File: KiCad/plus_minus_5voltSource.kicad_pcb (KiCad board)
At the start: 2 copper layers, 31.1 x 16.2 mm, 9 parts, among them P1 CONN_01X03, U1 7660

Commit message: Removed old PCB layout from the pcb file.
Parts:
- removed C1, C2: CP, Capacitors_ThroughHole:C_Radial_D5_L6_P2.5
- removed D1, D2: LED, LEDs:LED_0805
- removed G***: LOGO, PCB:AVO Logo
- removed P1: CONN_01X03, Pin_Headers:Pin_Header_Angled_1x03
- removed R1, R2: 1k, Resistors_SMD:R_0805_HandSoldering
- removed U1: 7660, Housings_DIP:DIP-8_W7.62mm
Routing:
- net GND: track 41.4 -> 0.00 mm
- net V-: track 31.6 -> 0.00 mm
- net Net-(D2-Pad2): track 20.2 -> 0.00 mm
- net VCC: track 15.4 -> 0.00 mm
- net Net-(C1-Pad1): track 6.92 -> 0.00 mm
- net Net-(C1-Pad2): track 5.85 -> 0.00 mm
- net Net-(D1-Pad1): track 3.62 -> 0.00 mm
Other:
- board outline removed
- board text removed: "+/-5V USB Power Supply V1.0"
- board text removed: "GND"
- board text removed: "V+"
- board text removed: "V-"
- board text removed: "avolabs.cc"

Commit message: Added pcb file to project.
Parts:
- added C3: C, Capacitors_ThroughHole:C_Disc_D3.0mm_W2.0mm_P2.50mm, F.Cu at (195.0, 94.9)
- added C4: C, Capacitors_ThroughHole:C_Disc_D3.0mm_W2.0mm_P2.50mm, F.Cu at (184.6, 105.6)
- added C5: C, Capacitors_ThroughHole:C_Disc_D3.0mm_W2.0mm_P2.50mm, F.Cu at (195.0, 101.5)
- added C6: C, Capacitors_ThroughHole:C_Disc_D3.0mm_W2.0mm_P2.50mm, F.Cu at (189.6, 105.6)
- added D1: LED, LEDs:LED_0805, F.Cu at (200.9, 94.0)
- added D2: LED, LEDs:LED_0805, F.Cu at (190.6, 111.4)
- added J1: USB_OTG, Connect:USB_Micro-B, F.Cu at (178.5, 106.5)
- added R1: 1k, Resistors_SMD:R_0805_HandSoldering, F.Cu at (185.9, 111.7)
- added R2: 1k, Resistors_SMD:R_0805_HandSoldering, F.Cu at (196.0, 107.6)
- added SW1: SW_Push, Buttons_Switches_ThroughHole:SW_PUSH_6mm, F.Cu at (185.5, 94.5)
- added U1: LM7805_TO220, TO_SOT_Packages_THT:TO-92_Inline_Narrow_Oval, F.Cu at (166.6, 110.4)
- added U2: 7660, Housings_DIP:DIP-8_W7.62mm, F.Cu at (163.4, 94.9)
- added U3: LM79L05_TO92, TO_SOT_Packages_THT:TO-92_Inline_Narrow_Oval, F.Cu at (176.8, 96.1)

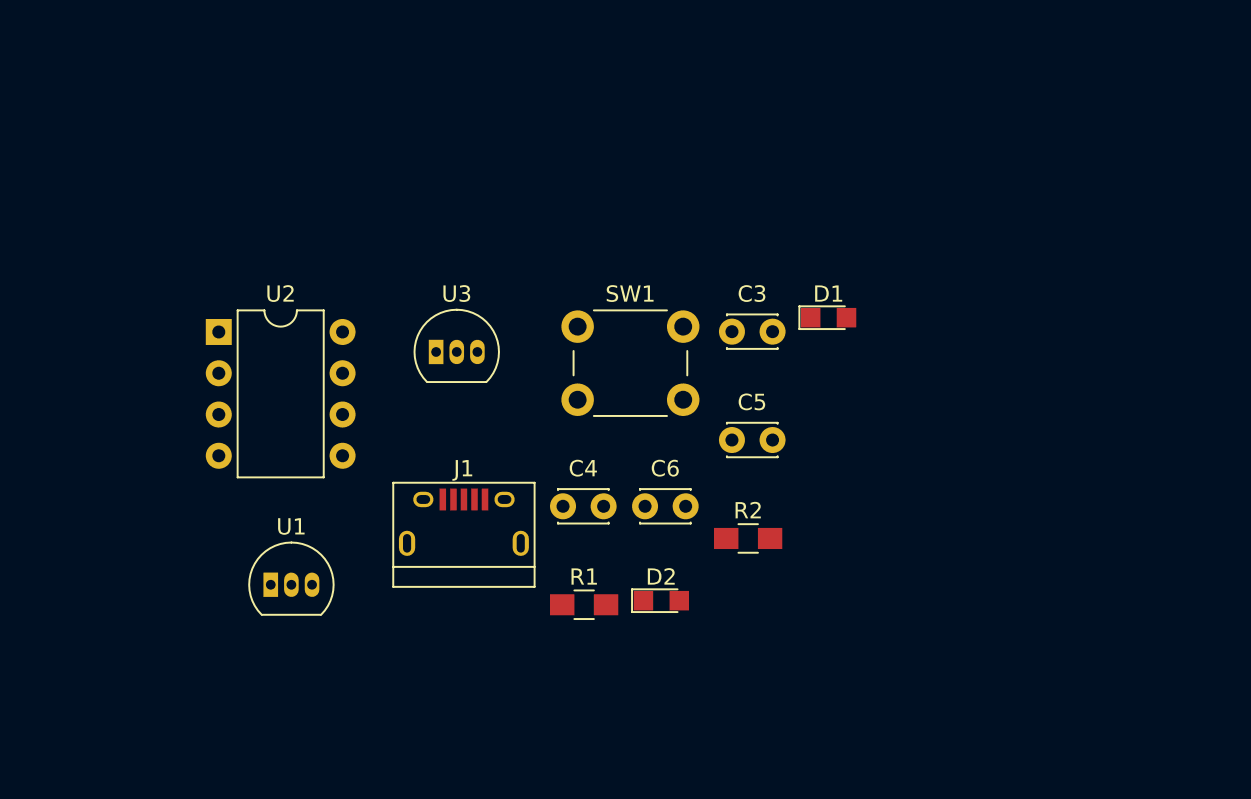
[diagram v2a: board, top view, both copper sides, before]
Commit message: Edited component association to be all through hole components.
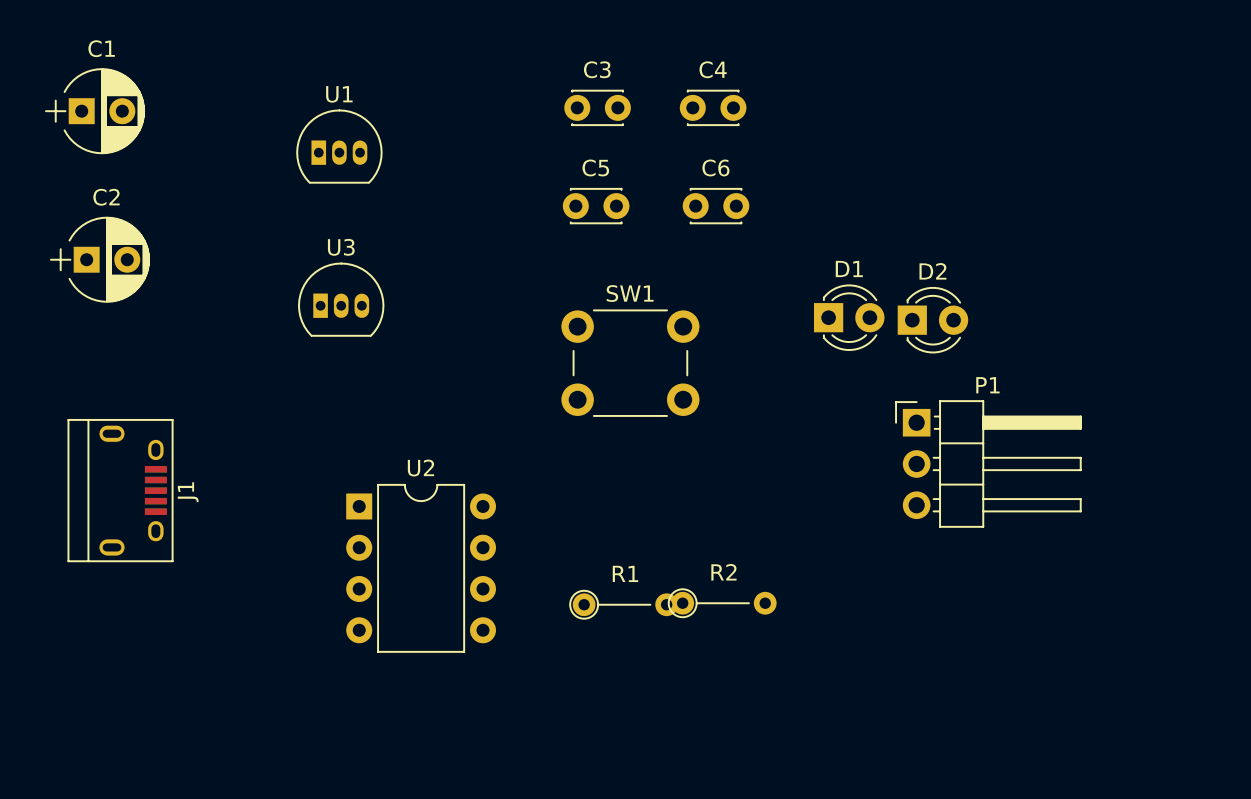
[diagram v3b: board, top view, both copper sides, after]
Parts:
- added C1: CP, Capacitors_ThroughHole:CP_Radial_D5.0mm_P2.50mm, F.Cu at (154.9, 81.3)
- added C2: CP, Capacitors_ThroughHole:CP_Radial_D5.0mm_P2.50mm, F.Cu at (155.2, 90.4)
- added P1: CONN_01X03, Pin_Headers:Pin_Header_Angled_1x03_Pitch2.54mm, F.Cu at (206.3, 100.5)
- D1, D2: footprint LEDs:LED_0805 -> LEDs:LED_D3.0mm
- R1, R2: footprint Resistors_SMD:R_0805_HandSoldering -> Resistors_ThroughHole:R_Axial_DIN0204_L3.6mm_D1.6mm_P5.08mm_Vertical
- moved U1 26.8 mm to (169.5, 83.8)
- moved C4 25.8 mm to (192.6, 81.1)
- moved D2 23.2 mm to (206.1, 94.1)
- moved J1 20.4 mm to (158.2, 104.6), turned to 270 degrees
- moved C6 18.7 mm to (192.7, 87.1)
- moved C5 17.3 mm to (185.4, 87.1)
- moved C3 16.7 mm to (185.4, 81.1)
- moved U2 13.8 mm to (172.0, 105.6)
- moved U3 7.66 mm to (169.6, 93.3)
- moved R2 5.67 mm to (191.9, 111.6)

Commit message: Formatted BOM.
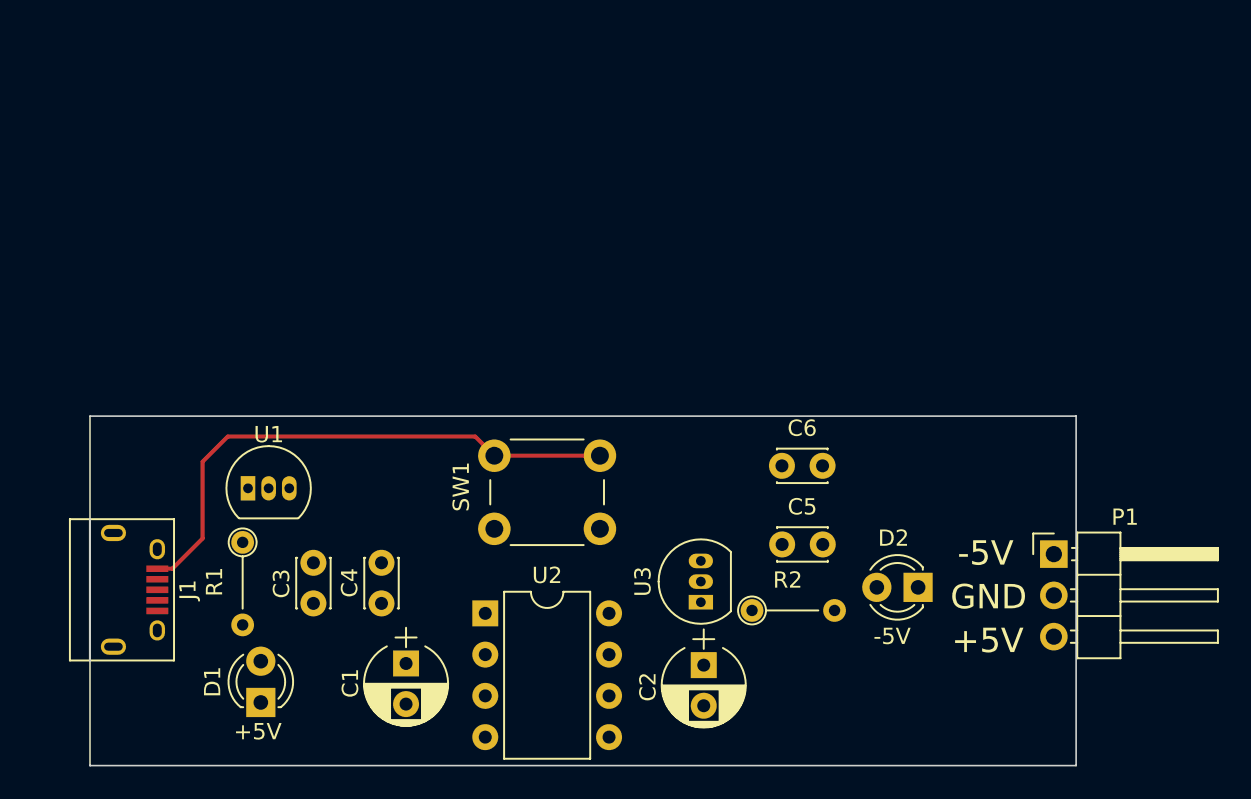
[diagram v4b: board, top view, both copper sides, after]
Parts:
- moved C2 45.4 mm to (193.2, 115.4), turned to 270 degrees
- moved D1 42.2 mm to (166.0, 117.7), turned to 90 degrees
- moved C1 39.4 mm to (174.9, 115.3), turned to 270 degrees
- moved C4 33.9 mm to (173.4, 109.1), turned to 270 degrees
- moved C3 32.4 mm to (169.2, 109.1), turned to 270 degrees
- moved U3 29.7 mm to (193.1, 111.5), turned to 90 degrees
- moved C5 24.4 mm to (198.1, 108.0)
- moved R1 21.4 mm to (164.8, 107.8), turned to 270 degrees
- moved U1 21.1 mm to (165.2, 104.5)
- moved C6 16.8 mm to (198.0, 103.1)
- moved D2 16.5 mm to (206.4, 110.6), turned to 180 degrees
- moved P1 11.7 mm to (214.8, 108.5)
- moved U2 10.2 mm to (179.8, 112.2)
- moved SW1 9.46 mm to (180.3, 102.5)
- moved J1 6.11 mm to (158.2, 110.7)
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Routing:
- net VCC: track 0.00 -> 33.9 mm
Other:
- board outline added: 60.7 x 21.5 mm
- board text added: "+5V"
- board text added: "-5V"
- board text added: "GND"

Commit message: Finalized pcb by adding edge cut, and routing to pcb.
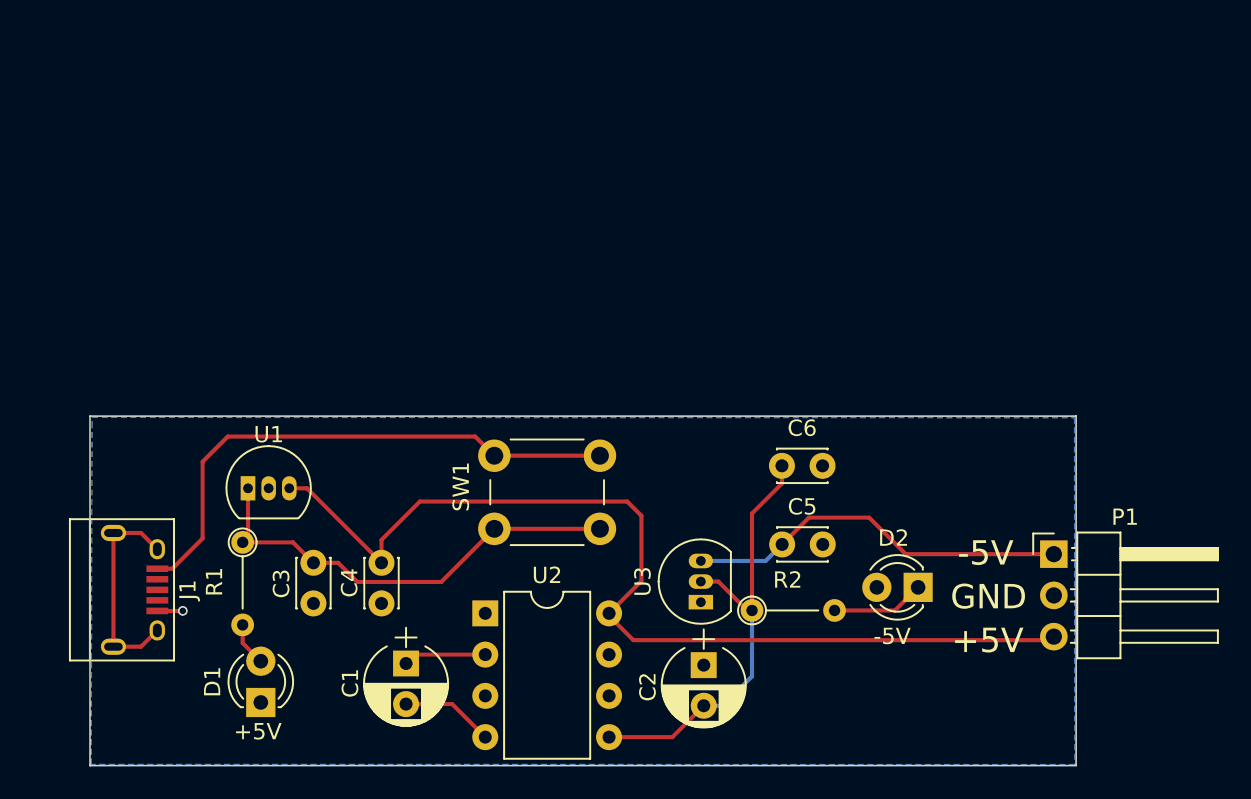
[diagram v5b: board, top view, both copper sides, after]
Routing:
- net Vpreg: track 0.00 -> 61.4 mm
- net V-: track 0.00 -> 28.0 mm
- net Net-(C3-Pad1): track 0.00 -> 27.8 mm
- net Vnreg: track 0.00 -> 23.8 mm
- net Net-(J1-Pad6): track 0.00 -> 13.2 mm
- net Net-(D2-Pad1): track 0.00 -> 5.73 mm
- net Net-(C1-Pad2): track 0.00 -> 5.72 mm
- net Net-(C1-Pad1): track 0.00 -> 5.10 mm
- net Net-(D1-Pad2): track 0.00 -> 2.70 mm
- net GND: track 0.00 -> 1.57 mm, vias 0 -> 1
- added copper zone on B.Cu, net GND
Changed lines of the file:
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@@
   (general
     (links 33)
-    (no_connects 31)
-    (area 155.397999 100.000599 219.772701 121.639801)
+    (no_connects 0)
+    (area 152.257 99.8263 225.557401 123.2168)
     (thickness 1.6)
     (drawings 9)
-    (tracks 7)
+    (tracks 62)
     (zones 0)
     (modules 16)
@@
     (effects (font (size 1 1) (thickness 0.2)))
   )
-  (segment (start 180.34 102.489) (end 186.84 102.489) (width 0.25) (layer F.Cu) (net 8) (status C00000))
-  (segment (start 159.592 109.444) (end 160.5199 109.444) (width 0.25) (layer F.Cu) (net 8) (status 400000))
-  (segment (start 179.1589 101.3079) (end 180.34 102.489) (width 0.25) (layer F.Cu) (net 8) (status 800000))
+  (segment (start 180.34 106.989) (end 186.84 106.989) (width 0.25) (layer F.Cu) (net 1))
+  (segment (start 169.2021 109.0803) (end 170.7261 109.0803) (width 0.25) (layer F.Cu) (net 1))
+  (segment (start 177.0676 110.2614) (end 180.34 106.989) (width 0.25) (layer F.Cu) (net 1))
+  (segment (start 171.9072 110.2614) (end 177.0676 110.2614) (width 0.25) (layer F.Cu) (net 1))
+  (segment (start 170.7261 109.0803) (end 171.9072 110.2614) (width 0.25) (layer F.Cu) (net 1))
+  (segment (start 164.846 107.823) (end 167.9448 107.823) (width 0.25) (layer F.Cu) (net 1))
+  (segment (start 167.9448 107.823) (end 169.2021 109.0803) (width 0.25) (layer F.Cu) (net 1))
+  (segment (start 165.1762 104.4956) (end 165.1762 107.4928) (width 0.25) (layer F.Cu) (net 1))
+  (segment (start 165.1762 107.4928) (end 164.846 107.823) (width 0.25) (layer F.Cu) (net 1))
+  (segment (start 159.592 112.044) (end 161.1549 112.044) (width 0.25) (layer F.Cu) (net 2) (status 400000))
+  (via (at 161.163 112.0394) (size 0.6) (drill 0.4) (layers F.Cu B.Cu) (net 2))
+  (segment (start 161.1595 112.0394) (end 161.163 112.0394) (width 0.25) (layer F.Cu) (net 2))
+  (segment (start 161.1549 112.044) (end 161.1595 112.0394) (width 0.25) (layer F.Cu) (net 2))
+  (segment (start 187.4012 112.1918) (end 187.4012 112.3442) (width 0.25) (layer F.Cu) (net 3))
+  (segment (start 187.4012 112.3442) (end 188.8998 113.8428) (width 0.25) (layer F.Cu) (net 3))
+  (segment (start 188.8998 113.8428) (end 214.5665 113.8428) (width 0.25) (layer F.Cu) (net 3))
+  (segment (start 214.5665 113.8428) (end 214.7824 113.6269) (width 0.25) (layer F.Cu) (net 3))
+  (segment (start 173.3931 109.0803) (end 173.3931 107.6706) (width 0.25) (layer F.Cu) (net 3))
+  (segment (start 189.3951 110.1979) (end 187.4012 112.1918) (width 0.25) (layer F.Cu) (net 3))
+  (segment (start 189.3951 106.1847) (end 189.3951 110.1979) (width 0.25) (layer F.Cu) (net 3))
+  (segment (start 188.5188 105.3084) (end 189.3951 106.1847) (width 0.25) (layer F.Cu) (net 3))
+  (segment (start 175.7553 105.3084) (end 188.5188 105.3084) (width 0.25) (layer F.Cu) (net 3))
+  (segment (start 173.3931 107.6706) (end 175.7553 105.3084) (width 0.25) (layer F.Cu) (net 3))
+  (segment (start 167.7162 104.4956) (end 168.8084 104.4956) (width 0.25) (layer F.Cu) (net 3))
+  (segment (start 168.8084 104.4956) (end 173.3931 109.0803) (width 0.25) (layer F.Cu) (net 3))
+  (segment (start 193.0527 108.966) (end 197.0405 108.966) (width 0.25) (layer B.Cu) (net 4))
+  (segment (start 197.0405 108.966) (end 198.0565 107.95) (width 0.25) (layer B.Cu) (net 4))
+  (segment (start 214.7824 108.5469) (end 205.6638 108.5469) (width 0.25) (layer F.Cu) (net 4))
+  (segment (start 199.7075 106.299) (end 198.0565 107.95) (width 0.25) (layer F.Cu) (net 4))
+  (segment (start 203.4159 106.299) (end 199.7075 106.299) (width 0.25) (layer F.Cu) (net 4))
+  (segment (start 205.6638 108.5469) (end 203.4159 106.299) (width 0.25) (layer F.Cu) (net 4))
+  (segment (start 193.2305 117.8795) (end 194.3881 117.8795) (width 0.25) (layer B.Cu) (net 5))
+  (segment (start 196.2023 116.0653) (end 196.2023 112.014) (width 0.25) (layer B.Cu) (net 5))
+  (segment (start 194.3881 117.8795) (end 196.2023 116.0653) (width 0.25) (layer B.Cu) (net 5))
+  (segment (start 198.0438 103.1113) (end 198.0438 104.2035) (width 0.25) (layer F.Cu) (net 5))
+  (segment (start 198.0438 104.2035) (end 196.2023 106.045) (width 0.25) (layer F.Cu) (net 5))
+  (segment (start 196.2023 106.045) (end 196.2023 112.014) (width 0.25) (layer F.Cu) (net 5))
+  (segment (start 196.2023 112.014) (end 195.9102 112.014) (width 0.25) (layer F.Cu) (net 5))
+  (segment (start 195.9102 112.014) (end 194.1322 110.236) (width 0.25) (layer F.Cu) (net 5))
+  (segment (start 194.1322 110.236) (end 193.0527 110.236) (width 0.25) (layer F.Cu) (net 5))
+  (segment (start 187.4012 119.8118) (end 191.2982 119.8118) (width 0.25) (layer F.Cu) (net 5))
+  (segment (start 191.2982 119.8118) (end 193.2305 117.8795) (width 0.25) (layer F.Cu) (net 5))
+  (segment (start 164.846 112.903) (end 164.846 114.0206) (width 0.25) (layer F.Cu) (net 6))
+  (segment (start 164.846 114.0206) (end 165.9636 115.1382) (width 0.25) (layer F.Cu) (net 6))
+  (segment (start 201.2823 112.014) (end 205.0034 112.014) (width 0.25) (layer F.Cu) (net 7))
+  (segment (start 205.0034 112.014) (end 206.4258 110.5916) (width 0.25) (layer F.Cu) (net 7))
+  (segment (start 180.34 102.489) (end 186.84 102.489) (width 0.25) (layer F.Cu) (net 8))
+  (segment (start 159.592 109.444) (end 160.5199 109.444) (width 0.25) (layer F.Cu) (net 8))
+  (segment (start 179.1589 101.3079) (end 180.34 102.489) (width 0.25) (layer F.Cu) (net 8))
   (segment (start 163.9316 101.3079) (end 179.1589 101.3079) (width 0.25) (layer F.Cu) (net 8))
   (segment (start 162.3822 102.8573) (end 163.9316 101.3079) (width 0.25) (layer F.Cu) (net 8))
   (segment (start 162.3822 107.5817) (end 162.3822 102.8573) (width 0.25) (layer F.Cu) (net 8))
   (segment (start 160.5199 109.444) (end 162.3822 107.5817) (width 0.25) (layer F.Cu) (net 8))
+  (segment (start 156.892 114.244) (end 156.892 107.244) (width 0.25) (layer F.Cu) (net 12))
+  (segment (start 156.892 114.244) (end 158.592 114.244) (width 0.25) (layer F.Cu) (net 12))
+  (segment (start 158.592 114.244) (end 159.592 113.244) (width 0.25) (layer F.Cu) (net 12))
+  (segment (start 156.892 107.244) (end 158.592 107.244) (width 0.25) (layer F.Cu) (net 12))
+  (segment (start 158.592 107.244) (end 159.592 108.244) (width 0.25) (layer F.Cu) (net 12))
+  (segment (start 179.7812 114.7318) (end 175.4505 114.7318) (width 0.25) (layer F.Cu) (net 14))
+  (segment (start 175.4505 114.7318) (end 174.9044 115.2779) (width 0.25) (layer F.Cu) (net 14))
+  (segment (start 174.9044 117.7779) (end 177.7473 117.7779) (width 0.25) (layer F.Cu) (net 17))
+  (segment (start 177.7473 117.7779) (end 179.7812 119.8118) (width 0.25) (layer F.Cu) (net 17))
+  (zone (net 2) (net_name GND) (layer B.Cu) (hatch edge 0.508)
+    (connect_pads (clearance 0.508))
+    (min_thickness 0.254)
+    (fill yes (arc_segments 16) (thermal_gap 0.508) (thermal_bridge_width 0.508))
+    (polygon
+      (pts
+        (xy 216.0524 100.1522) (xy 216.0778 121.5009) (xy 155.5242 121.4882) (xy 155.575 100.7237) (xy 155.575 100.1268)
+      )
+    )
+  )
 )

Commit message: Added logo to PCB. Generated gerbers, and board images. Changed name of board to Orion.
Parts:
- added logo: , logo:logo, B.Cu at (202.5, 102.9)
